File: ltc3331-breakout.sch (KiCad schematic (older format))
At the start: 58 parts, among them IC1 LTC3331, J1 CONN_01X03, J10 CONN_01X03, J11 CONN_01X03, J12 CONN_01X03, J13 CONN_01X04, J14 CONN_02X08, J15 CONN_02X08, J16 CONN_02X08, J17 CONN_02X08, J18 CONN_02X04, J19 CONN_02X05, J2 CONN_01X03, J3 CONN_01X03, J4 CONN_01X04, J5 CONN_01X03, J6 CONN_01X03, J7 CONN_01X03, J8 CONN_01X04, J9 CONN_01X02_FEMALE

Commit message: schematic cleanup
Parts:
- removed J19: CONN_02X05, Pin_Headers:Pin_Header_Straight_2x05_Pitch2.54mm, symbol CONN_02X05
- added J14: CONN_02X10, symbol CONN_02X10
- added R2: 10, Resistors_SMD:R_1206_HandSoldering, symbol R
- C1: value 4.7uF 6.3V -> 1uF 6.3V
- R1: value DNP -> 3K
- renumbered J4 to J1, J13 to J10, J12 to J11, J10 to J12, J11 to J13, J14 to J15, J15 to J16, J16 to J17, J17 to J18, J18 to J19, J3 to J2, J1 to J3, J2 to J4, J8 to J5, J7 to J6, J5 to J7, J6 to J8, R2 to R3
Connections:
- wire segments 231 -> 242
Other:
- moved on the sheet: BT1, BT2, C1, C2, C3, C4, C5, C6, C7, J1, J10, J11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

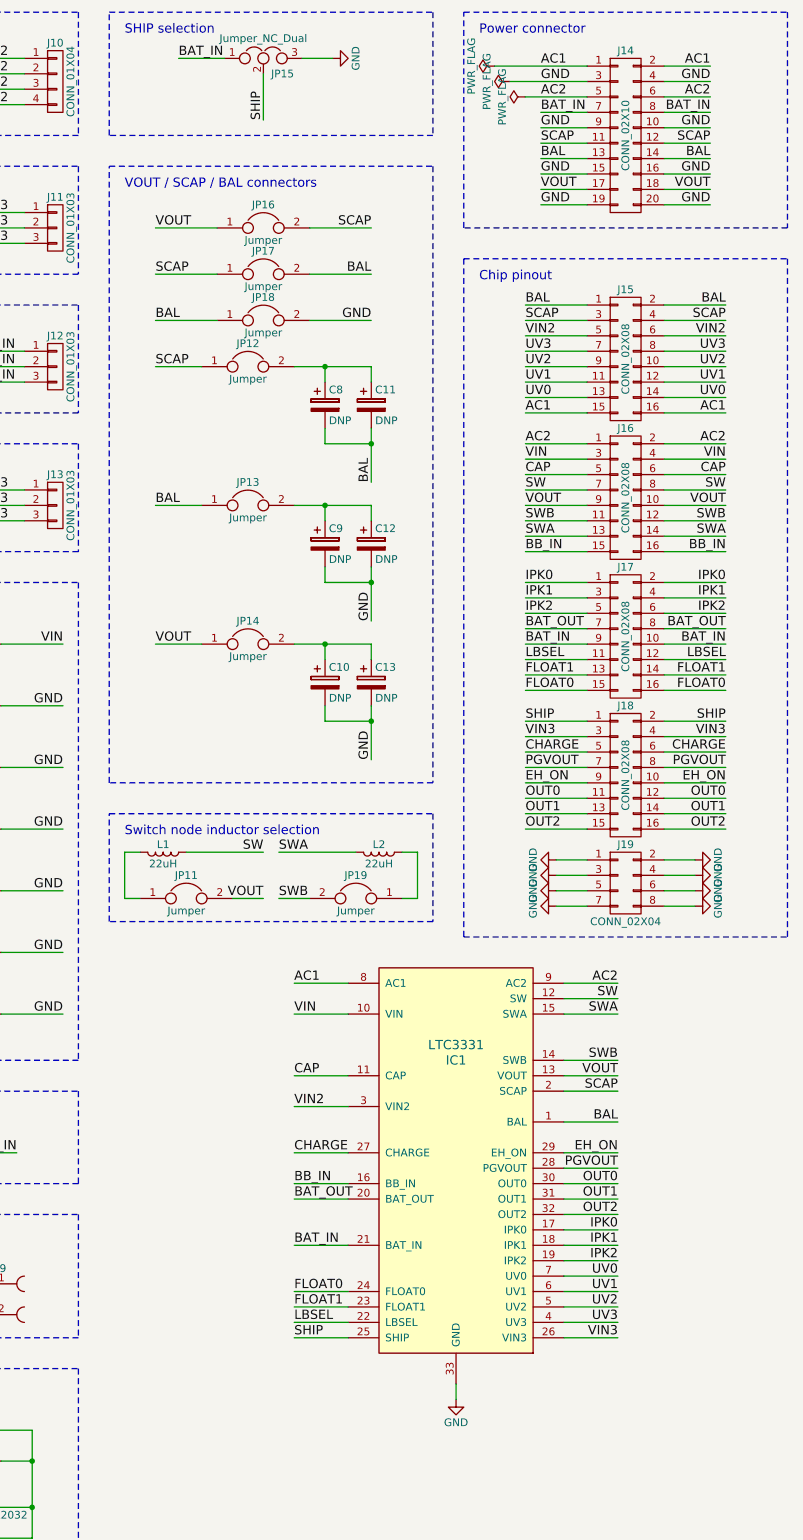
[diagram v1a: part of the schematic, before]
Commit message: added level shifter for PGOOD, EHORBAT; cleanup; most footprints
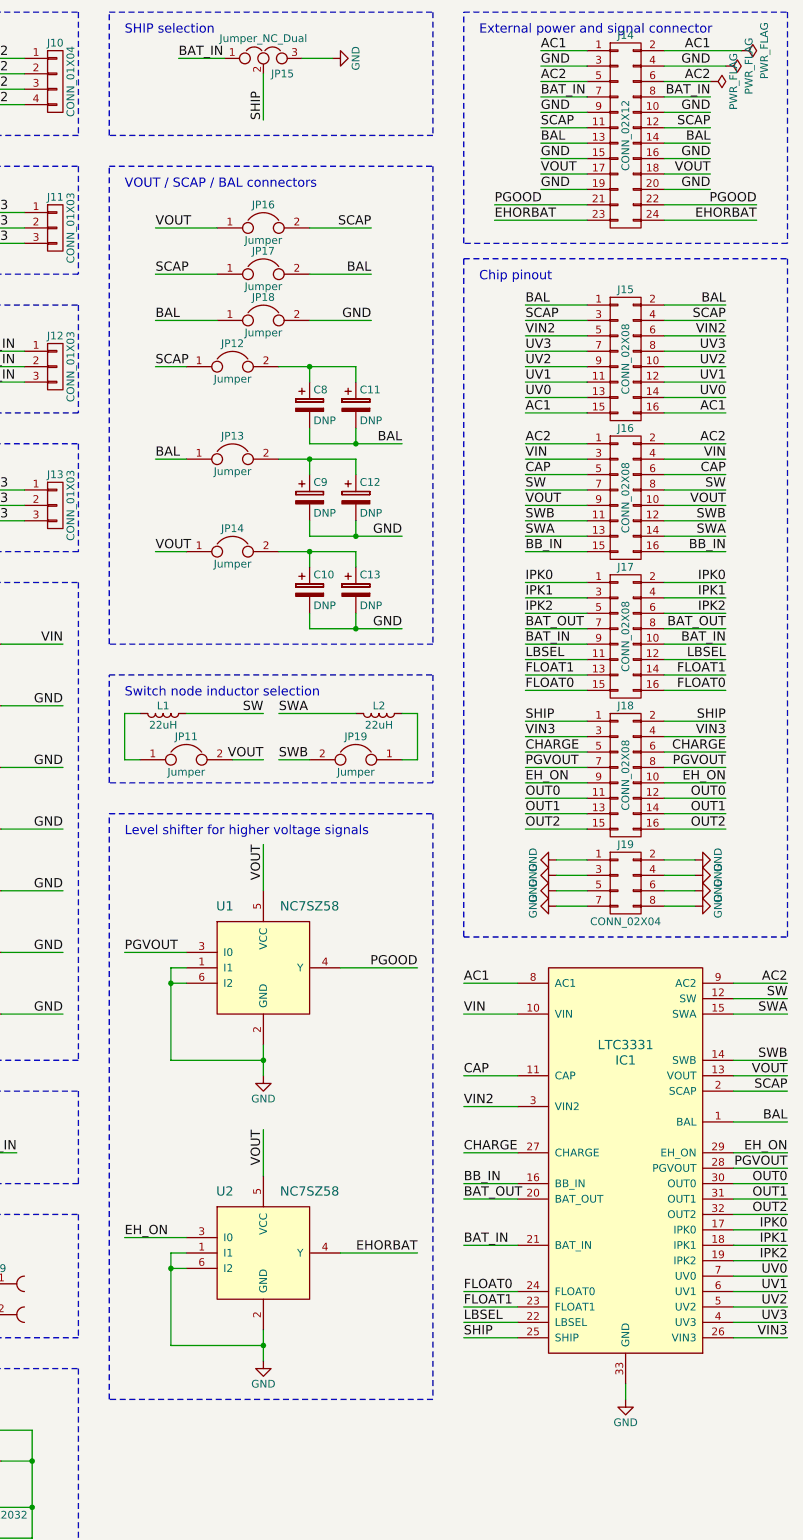
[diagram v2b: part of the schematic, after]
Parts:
- removed J14: CONN_02X10, symbol CONN_02X10
- added J14: CONN_02X12, Pin_Headers:Pin_Header_Straight_2x12_Pitch2.54mm, symbol CONN_02X12
- added U1, U2: NC7SZ58, TO_SOT_Packages_SMD:SOT-363_SC-70-6_Handsoldering, symbol NC7SZ58
- C10, C11, C12, C13, C8, C9: footprint (none) -> Capacitors_SMD:CP_Elec_10x10
- L1, L2: footprint (none) -> Inductors:Inductor_Wurth_HCI-1890
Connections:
- net AC1: now also J14.1 (P1), J14.2 (P2)
- net AC2: now also J14.5 (P5), J14.6 (P6)
- net BAL: now also J14.13 (P13), J14.14 (P14)
- net BAT_IN: now also J14.7 (P7), J14.8 (P8)
- net EH_ON: now also U2.3 (I0)
- net GND: now also J14.10 (P10), J14.15 (P15), J14.16 (P16), J14.19 (P19), J14.20 (P20), J14.3 (P3), J14.4 (P4), J14.9 (P9), U1.1 (I1), U1.2 (GND), U1.6 (I2), U2.1 (I1), U2.2 (GND), U2.6 (I2)
- net PGVOUT: now also U1.3 (I0)
- net SCAP: now also J14.11 (P11), J14.12 (P12)
- net VOUT: now also J14.17 (P17), J14.18 (P18), U1.5 (VCC), U2.5 (VCC)
- new net EHORBAT: J14.23 (P23), J14.24 (P24), U2.4 (Y)
- new net PGOOD: J14.21 (P21), J14.22 (P22), U1.4 (Y)
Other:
- note added: "External power and signal connector"
- note added: "Level shifter for higher voltage signals"
- note removed: "Power connector"
- moved on the sheet: C10, C11, C12, C13, C8, C9, IC1, JP11, JP12, JP13, JP14, JP19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

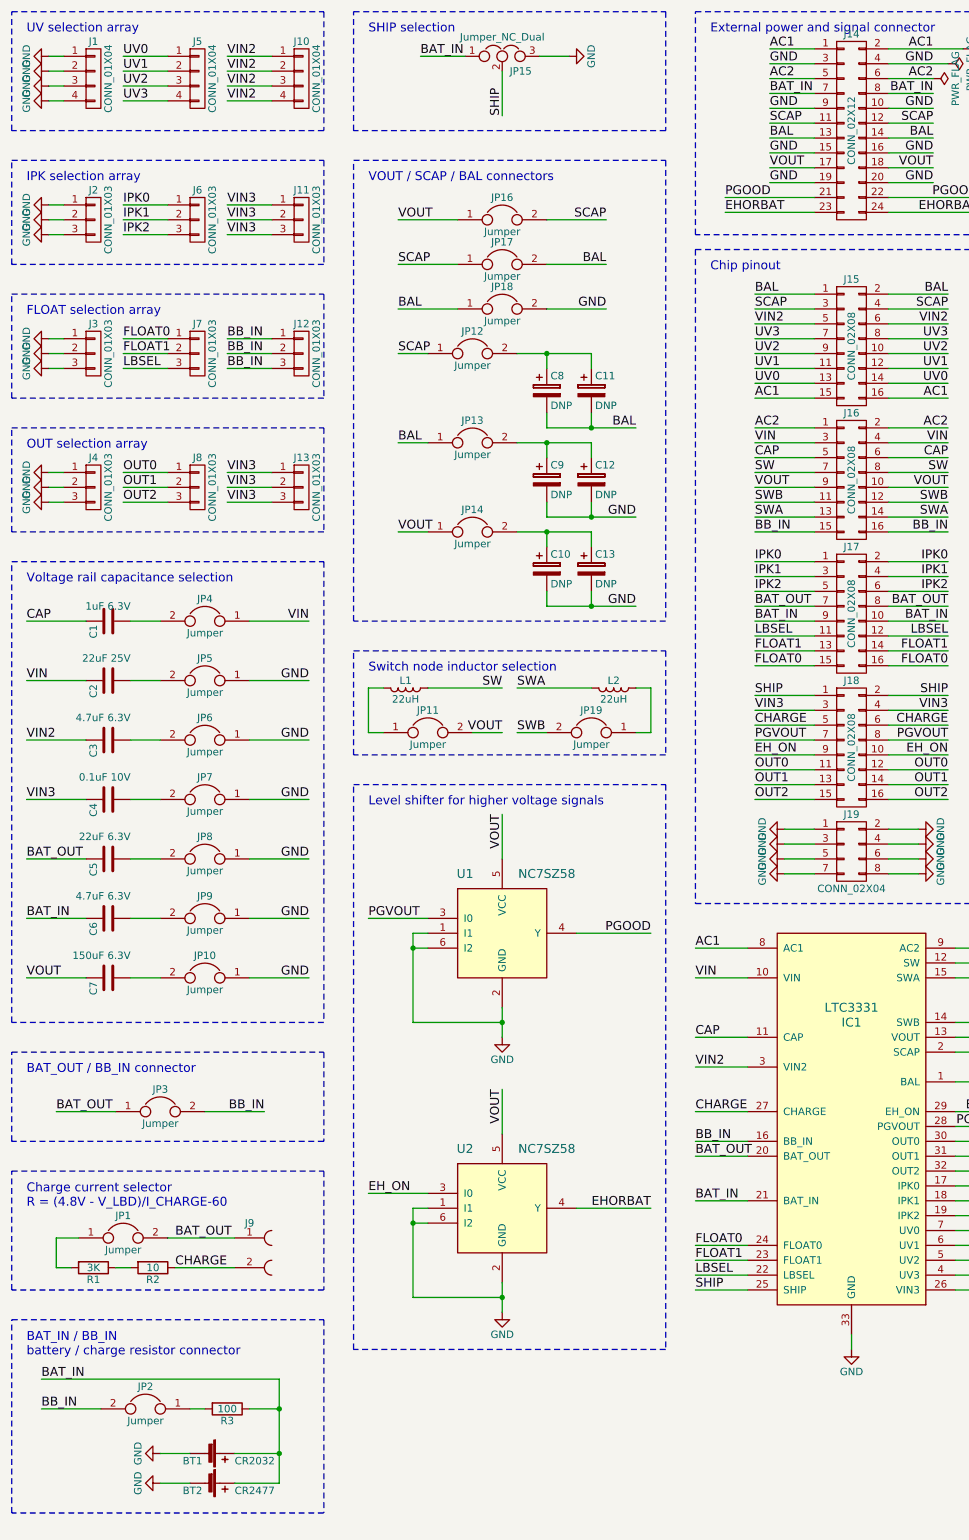
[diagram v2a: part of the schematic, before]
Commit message: use lipo-connector instead of CR2477. cleanup.
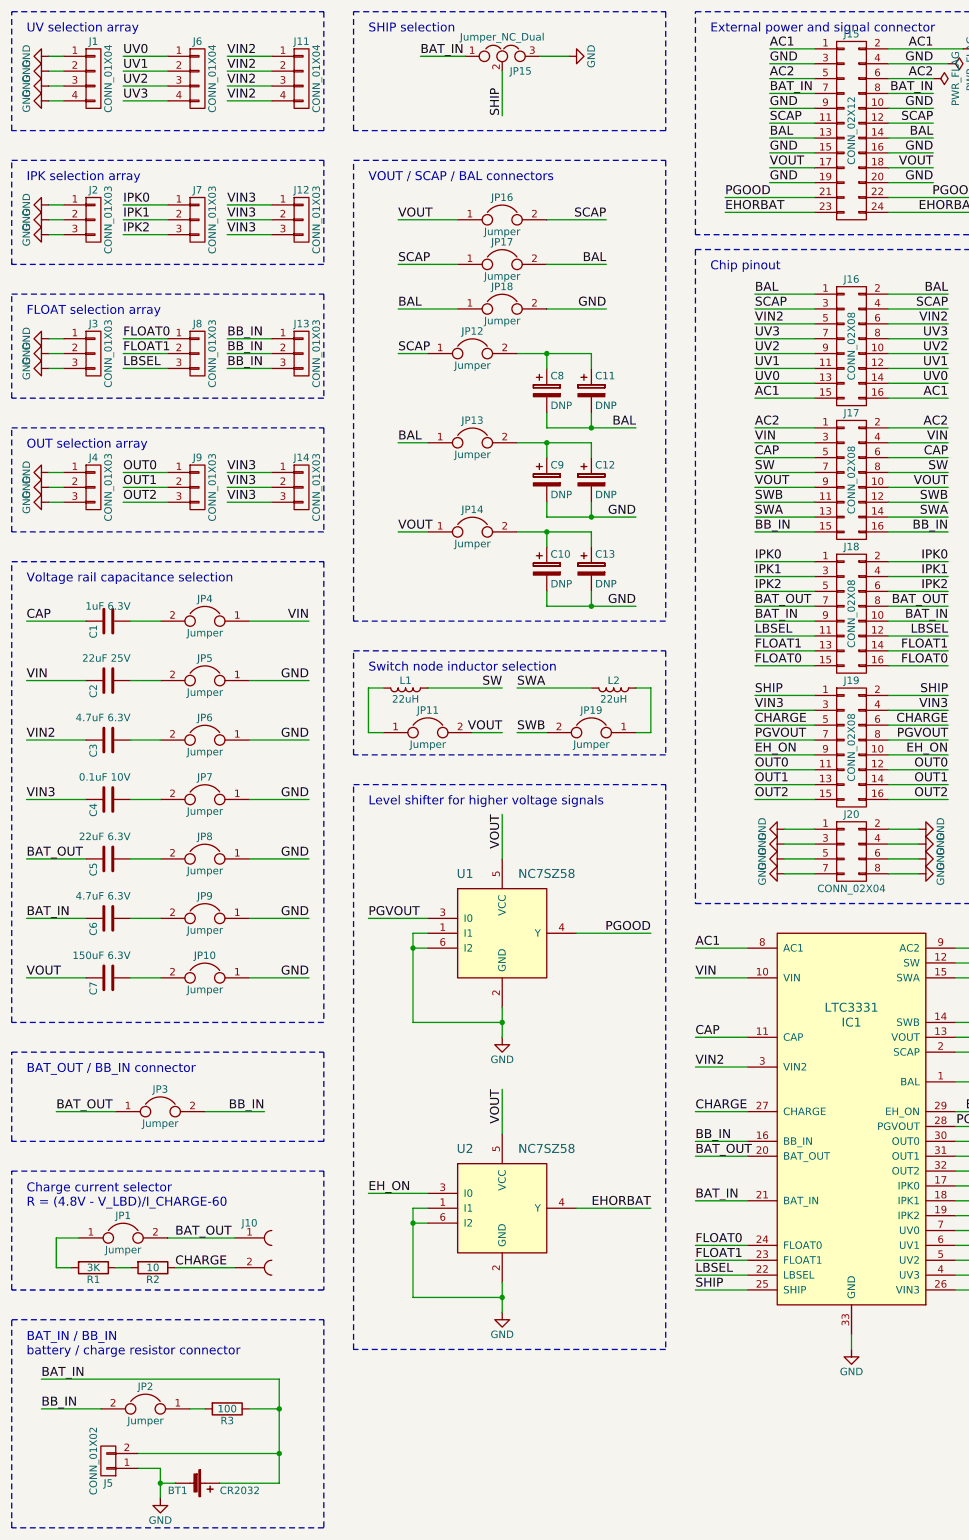
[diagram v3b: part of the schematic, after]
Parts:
- removed BT2: CR2477, symbol Battery_Cell
- added J5: CONN_01X02, Pin_Headers:Pin_Header_Straight_1x02_Pitch2.54mm, symbol CONN_01X02
- renumbered J9 to J10, J10 to J11, J11 to J12, J12 to J13, J13 to J14, J14 to J15, J15 to J16, J16 to J17, J17 to J18, J18 to J19, J19 to J20, J5 to J6, J6 to J7, J7 to J8, J8 to J9
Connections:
- net BAT_IN: now also J5.2 (P2)
- net GND: now also J5.1 (P1)
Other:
- moved on the sheet: BT1
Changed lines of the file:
@@
 EH_ON
 $Comp
-L CONN_01X03 J13
+L CONN_01X03 J14
 U 1 1 595A3B36
 P 2750 3900
-F 0 "J13" H 2750 4100 50  0000 C CNN
+F 0 "J14" H 2750 4100 50  0000 C CNN
 F 1 "CONN_01X03" V 2850 3900 50  0000 C CNN
 F 2 "Pin_Headers:Pin_Header_Straight_1x03_Pitch2.54mm" H 2750 3900 50  0001 C CNN
@@
 $EndComp
 $Comp
-L CONN_01X03 J8
+L CONN_01X03 J9
 U 1 1 595A3B2F
 P 2050 3900
-F 0 "J8" H 2050 4100 50  0000 C CNN
+F 0 "J9" H 2050 4100 50  0000 C CNN
 F 1 "CONN_01X03" V 2150 3900 50  0000 C CNN
 F 2 "Pin_Headers:Pin_Header_Straight_1x03_Pitch2.54mm" H 2050 3900 50  0001 C CNN
@@
 OUT selection array
 $Comp
-L CONN_01X03 J11
+L CONN_01X03 J12
 U 1 1 595A6241
 P 2750 2100
-F 0 "J11" H 2750 2300 50  0000 C CNN
+F 0 "J12" H 2750 2300 50  0000 C CNN
 F 1 "CONN_01X03" V 2850 2100 50  0000 C CNN
 F 2 "Pin_Headers:Pin_Header_Straight_1x03_Pitch2.54mm" H 2750 2100 50  0001 C CNN
@@
 $EndComp
 $Comp
-L CONN_01X03 J6
+L CONN_01X03 J7
 U 1 1 595A6263
 P 2050 2100
-F 0 "J6" H 2050 2300 50  0000 C CNN
+F 0 "J7" H 2050 2300 50  0000 C CNN
 F 1 "CONN_01X03" V 2150 2100 50  0000 C CNN
 F 2 "Pin_Headers:Pin_Header_Straight_1x03_Pitch2.54mm" H 2050 2100 50  0001 C CNN
@@
 $EndComp
 $Comp
-L CONN_01X04 J5
+L CONN_01X04 J6
 U 1 1 595A7074
 P 2050 1150
-F 0 "J5" H 2050 1400 50  0000 C CNN
+F 0 "J6" H 2050 1400 50  0000 C CNN
 F 1 "CONN_01X04" V 2150 1150 50  0000 C CNN
 F 2 "Pin_Headers:Pin_Header_Straight_1x04_Pitch2.54mm" H 2050 1150 50  0001 C CNN
@@
 $EndComp
 $Comp
-L CONN_01X04 J10
+L CONN_01X04 J11
 U 1 1 595A708E
 P 2750 1150
-F 0 "J10" H 2750 1400 50  0000 C CNN
+F 0 "J11" H 2750 1400 50  0000 C CNN
 F 1 "CONN_01X04" V 2850 1150 50  0000 C CNN
 F 2 "Pin_Headers:Pin_Header_Straight_1x04_Pitch2.54mm" H 2750 1150 50  0001 C CNN
@@
 BB_IN
 $Comp
-L CONN_01X03 J12
+L CONN_01X03 J13
 U 1 1 595A9E54
 P 2750 3000
-F 0 "J12" H 2750 3200 50  0000 C CNN
+F 0 "J13" H 2750 3200 50  0000 C CNN
 F 1 "CONN_01X03" V 2850 3000 50  0000 C CNN
 F 2 "Pin_Headers:Pin_Header_Straight_1x03_Pitch2.54mm" H 2750 3000 50  0001 C CNN
@@
 BB_IN
 $Comp
-L CONN_01X03 J7
+L CONN_01X03 J8
 U 1 1 595A9E74
 P 2050 3000
-F 0 "J7" H 2050 3200 50  0000 C CNN
+F 0 "J8" H 2050 3200 50  0000 C CNN
 F 1 "CONN_01X03" V 2150 3000 50  0000 C CNN
 F 2 "Pin_Headers:Pin_Header_Straight_1x03_Pitch2.54mm" H 2050 3000 50  0001 C CNN
@@
 BB_IN
 $Comp
-L CONN_01X02_FEMALE J9
+L CONN_01X02_FEMALE J10
 U 1 1 595C3F70
 P 2400 9050
-F 0 "J9" H 2400 9250 50  0000 C CNN
+F 0 "J10" H 2400 9250 50  0000 C CNN
 F 1 "CONN_01X02_FEMALE" H 2300 8850 50  0001 C CNN
 F 2 "Pin_Headers:Pin_Header_Straight_1x02_Pitch2.54mm" H 2400 9150 50  0001 C CNN
@@
 VIN
 $Comp
-L CONN_02X08 J15
+L CONN_02X08 J16
 U 1 1 595D4745
 P 6450 2950
-F 0 "J15" H 6450 3400 50  0000 C CNN
+F 0 "J16" H 6450 3400 50  0000 C CNN
 F 1 "CONN_02X08" V 6450 2950 50  0000 C CNN
 F 2 "Pin_Headers:Pin_Header_Straight_2x08_Pitch2.54mm" H 6450 1750 50  0001 C CNN
@@
 AC1
 $Comp
-L CONN_02X08 J18
+L CONN_02X08 J19
 U 1 1 595D4A65
 P 6450 5650
-F 0 "J18" H 6450 6100 50  0000 C CNN
+F 0 "J19" H 6450 6100 50  0000 C CNN
 F 1 "CONN_02X08" V 6450 5650 50  0000 C CNN
 F 2 "Pin_Headers:Pin_Header_Straight_2x08_Pitch2.54mm" H 6450 4450 50  0001 C CNN
@@
 OUT2
 $Comp
-L CONN_02X08 J16
+L CONN_02X08 J17
 U 1 1 595D4FF6
 P 6450 3850
-F 0 "J16" H 6450 4300 50  0000 C CNN
+F 0 "J17" H 6450 4300 50  0000 C CNN
 F 1 "CONN_02X08" V 6450 3850 50  0000 C CNN
 F 2 "Pin_Headers:Pin_Header_Straight_2x08_Pitch2.54mm" H 6450 2650 50  0001 C CNN
@@
 $EndComp
 $Comp
-L CONN_02X08 J17
+L CONN_02X08 J18
 U 1 1 595D50FE
 P 6450 4750
-F 0 "J17" H 6450 5200 50  0000 C CNN
+F 0 "J18" H 6450 5200 50  0000 C CNN
 F 1 "CONN_02X08" V 6450 4750 50  0000 C CNN
 F 2 "Pin_Headers:Pin_Header_Straight_2x08_Pitch2.54mm" H 6450 3550 50  0001 C CNN
@@
 $EndComp
 $Comp
-L CONN_02X04 J19
+L CONN_02X04 J20
 U 1 1 595D6B13
 P 6450 6350
-F 0 "J19" H 6450 6600 50  0000 C CNN
+F 0 "J20" H 6450 6600 50  0000 C CNN
 F 1 "CONN_02X04" H 6450 6100 50  0000 C CNN
 F 2 "Pin_Headers:Pin_Header_Straight_2x04_Pitch2.54mm" H 6450 5150 50  0001 C CNN
@@
 L GND #PWR024
 U 1 1 595E0E2E
-P 1800 10400
-F 0 "#PWR024" H 1800 10150 50  0001 C CNN
-F 1 "GND" H 1800 10250 50  0000 C CNN
-F 2 "" H 1800 10400 50  0001 C CNN
-F 3 "" H 1800 10400 50  0001 C CNN
-	1    1800 10400
-	0    1    1    0
+P 1800 10700
+F 0 "#PWR024" H 1800 10450 50  0001 C CNN
+F 1 "GND" H 1800 10550 50  0000 C CNN
+F 2 "" H 1800 10700 50  0001 C CNN
+F 3 "" H 1800 10700 50  0001 C CNN
+	1    1800 10700
+	1    0    0    -1
 $EndComp
 $Comp
 L Battery_Cell BT1
 U 1 1 595E153E
-P 2100 10400
-F 0 "BT1" V 2150 10250 50  0000 L CNN
-F 1 "CR2032" V 2150 10600 50  0000 L CNN
-F 2 "footprints:SMTU-2032-LF" V 2100 10460 50  0001 C CNN
-F 3 "http://www.farnell.com/datasheets/1678381.pdf" V 2100 10460 50  0001 C CNN
-F 4 "1216354" V 2100 10400 60  0001 C CNN "Farnell"
-	1    2100 10400
-	0    1    1    0
-$EndComp
-$Comp
-L GND #PWR025
-U 1 1 595E1E2C
-P 1800 10600
-F 0 "#PWR025" H 1800 10350 50  0001 C CNN
-F 1 "GND" H 1800 10450 50  0000 C CNN
-F 2 "" H 1800 10600 50  0001 C CNN
-F 3 "" H 1800 10600 50  0001 C CNN
-	1    1800 10600
-	0    1    1    0
-$EndComp
-$Comp
-L Battery_Cell BT2
-U 1 1 595E1E32
-P 2100 10600
-F 0 "BT2" V 2150 10450 50  0000 L CNN
-F 1 "CR2477" V 2150 10800 50  0000 L CNN
-F 2 "" V 2100 10660 50  0001 C CNN
-F 3 "" V 2100 10660 50  0001 C CNN
-	1    2100 10600
+P 2000 10600
+F 0 "BT1" V 2050 10450 50  0000 L CNN
+F 1 "CR2032" V 2050 10800 50  0000 L CNN
+F 2 "footprints:SMTU-2032-LF" V 2000 10660 50  0001 C CNN
+F 3 "http://www.farnell.com/datasheets/1678381.pdf" V 2000 10660 50  0001 C CNN
+F 4 "1216354" V 2000 10600 60  0001 C CNN "Farnell"
+	1    2000 10600
 	0    1    1    0
 $EndComp
@@
 GND
 $Comp
-L PWR_FLAG #FLG026
+L PWR_FLAG #FLG025
 U 1 1 595F25F2
 P 7100 1050
-F 0 "#FLG026" H 7100 1125 50  0001 C CNN
+F 0 "#FLG025" H 7100 1125 50  0001 C CNN
 F 1 "PWR_FLAG" H 7100 1200 50  0000 C CNN
 F 2 "" H 7100 1050 50  0001 C CNN
@@
 $EndComp
 $Comp
-L PWR_FLAG #FLG027
+L PWR_FLAG #FLG026
 U 1 1 595F27FA
 P 7200 950
-F 0 "#FLG027" H 7200 1025 50  0001 C CNN
+F 0 "#FLG026" H 7200 1025 50  0001 C CNN
 F 1 "PWR_FLAG" H 7200 1100 50  0000 C CNN
 F 2 "" H 7200 950 50  0001 C CNN
@@
 $EndComp
 $Comp
-L PWR_FLAG #FLG028
+L PWR_FLAG #FLG027
 U 1 1 595F2A04
 P 7000 1150
-F 0 "#FLG028" H 7000 1225 50  0001 C CNN
+F 0 "#FLG027" H 7000 1225 50  0001 C CNN
 F 1 "PWR_FLAG" H 7000 1300 50  0000 C CNN
 F 2 "" H 7000 1150 50  0001 C CNN
@@
 	800  9500 2900 9500
 Wire Notes Line
-	2900 9500 2900 10800
-Wire Notes Line
-	800  10800 800  9500
-Wire Notes Line
-	2900 10800 800  10800
+	2900 9500 2900 10900
+Wire Notes Line
+	800  10900 800  9500
+Wire Notes Line
+	2900 10900 800  10900
 Wire Wire Line
 	1800 6800 1600 6800
@@
 	2600 9900 2600 10600
 Wire Wire Line
-	1800 10400 2000 10400
-Wire Wire Line
-	1800 10600 2000 10600
-Wire Wire Line
-	2600 10600 2300 10600
+	2600 10600 2200 10600
 Connection ~ 2600 10100
 Wire Wire Line
-	2300 10400 2600 10400
+	1650 10400 2600 10400
 Connection ~ 2600 10400
 Wire Notes Line
@@
 $EndComp
 $Comp
-L GND #PWR029
+L GND #PWR028
 U 1 1 595B5AD1
 P 4100 7600
-F 0 "#PWR029" H 4100 7350 50  0001 C CNN
+F 0 "#PWR028" H 4100 7350 50  0001 C CNN
 F 1 "GND" H 4100 7450 50  0000 C CNN
 F 2 "" H 4100 7600 50  0001 C CNN
@@
 $EndComp
 $Comp
-L GND #PWR030
+L GND #PWR029
 U 1 1 595B6DD5
 P 4100 9450
-F 0 "#PWR030" H 4100 9200 50  0001 C CNN
+F 0 "#PWR029" H 4100 9200 50  0001 C CNN
 F 1 "GND" H 4100 9300 50  0000 C CNN
 F 2 "" H 4100 9450 50  0001 C CNN
@@
 EHORBAT
 $Comp
-L CONN_02X12 J14
+L CONN_02X12 J15
 U 1 1 595BED1F
 P 6450 1500
-F 0 "J14" H 6450 2150 50  0000 C CNN
+F 0 "J15" H 6450 2150 50  0000 C CNN
 F 1 "CONN_02X12" V 6450 1500 50  0000 C CNN
 F 2 "Pin_Headers:Pin_Header_Straight_2x12_Pitch2.54mm" H 6450 300 50  0001 C CNN
@@
 	1    0    0    -1
 $EndComp
+$Comp
+L CONN_01X02 J5
+U 1 1 595BF82D
+P 1450 10450
+F 0 "J5" H 1450 10600 50  0000 C CNN
+F 1 "CONN_01X02" V 1550 10450 50  0000 C CNN
+F 2 "Pin_Headers:Pin_Header_Straight_1x02_Pitch2.54mm" H 1450 10450 50  0001 C CNN
+F 3 "" H 1450 10450 50  0001 C CNN
+	1    1450 10450
+	-1   0    0    1
+$EndComp
+Wire Wire Line
+	1900 10600 1800 10600
+Wire Wire Line
+	1800 10500 1800 10700
+Wire Wire Line
+	1800 10500 1650 10500
+Connection ~ 1800 10600
 $EndSCHEMATC

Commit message: replace 22uF inductor footprints with better ones
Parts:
- L1, L2: footprint Inductors:Inductor_Wurth_HCI-1890 -> Inductors:Inductor_Taiyo-Yuden_NR-30xx_HandSoldering
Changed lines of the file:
@@
 F 0 "L2" V 4800 5250 50  0000 C CNN
 F 1 "22uH" V 4925 5250 50  0000 C CNN
-F 2 "Inductors:Inductor_Wurth_HCI-1890" H 4850 5250 50  0001 C CNN
+F 2 "Inductors:Inductor_Taiyo-Yuden_NR-30xx_HandSoldering" H 4850 5250 50  0001 C CNN
 F 3 "" H 4850 5250 50  0001 C CNN
 	1    4850 5250
@@
 F 0 "L1" V 3400 5250 50  0000 C CNN
 F 1 "22uH" V 3525 5250 50  0000 C CNN
-F 2 "Inductors:Inductor_Wurth_HCI-1890" H 3450 5250 50  0001 C CNN
+F 2 "Inductors:Inductor_Taiyo-Yuden_NR-30xx_HandSoldering" H 3450 5250 50  0001 C CNN
 F 3 "" H 3450 5250 50  0001 C CNN
 	1    3450 5250
